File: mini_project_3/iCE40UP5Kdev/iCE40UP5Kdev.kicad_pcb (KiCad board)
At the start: 2 copper layers, 27.2 x 52.8 mm, 51 parts, among them J1 USB4105-GF-A, J2 Left, J3 Right, U1 W25Q32JV, U2 MIC5365-1-2YD5, U3 MIC5318-3-3YD5, U4 ICE40UP5K-SG48ITR, X1 IQXO-791

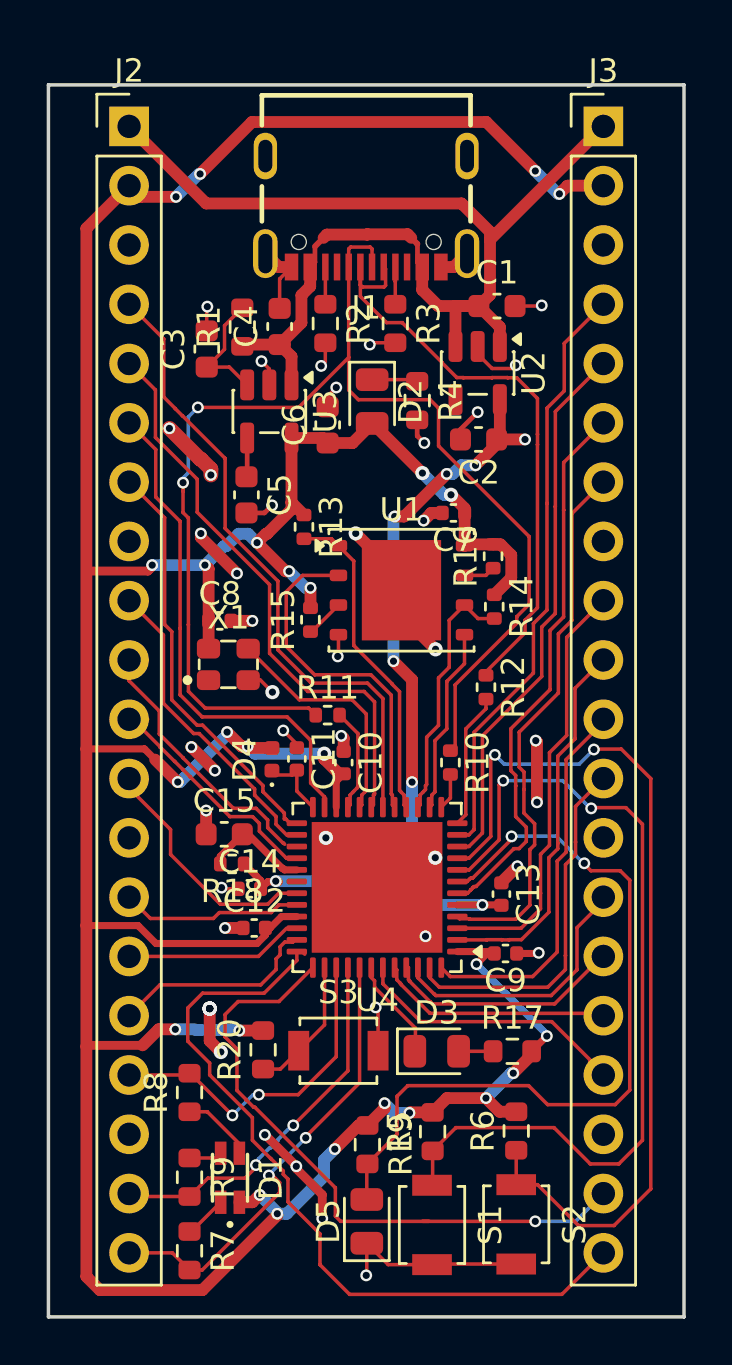
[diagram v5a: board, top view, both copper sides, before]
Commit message: Add silkscreen to mini project 3
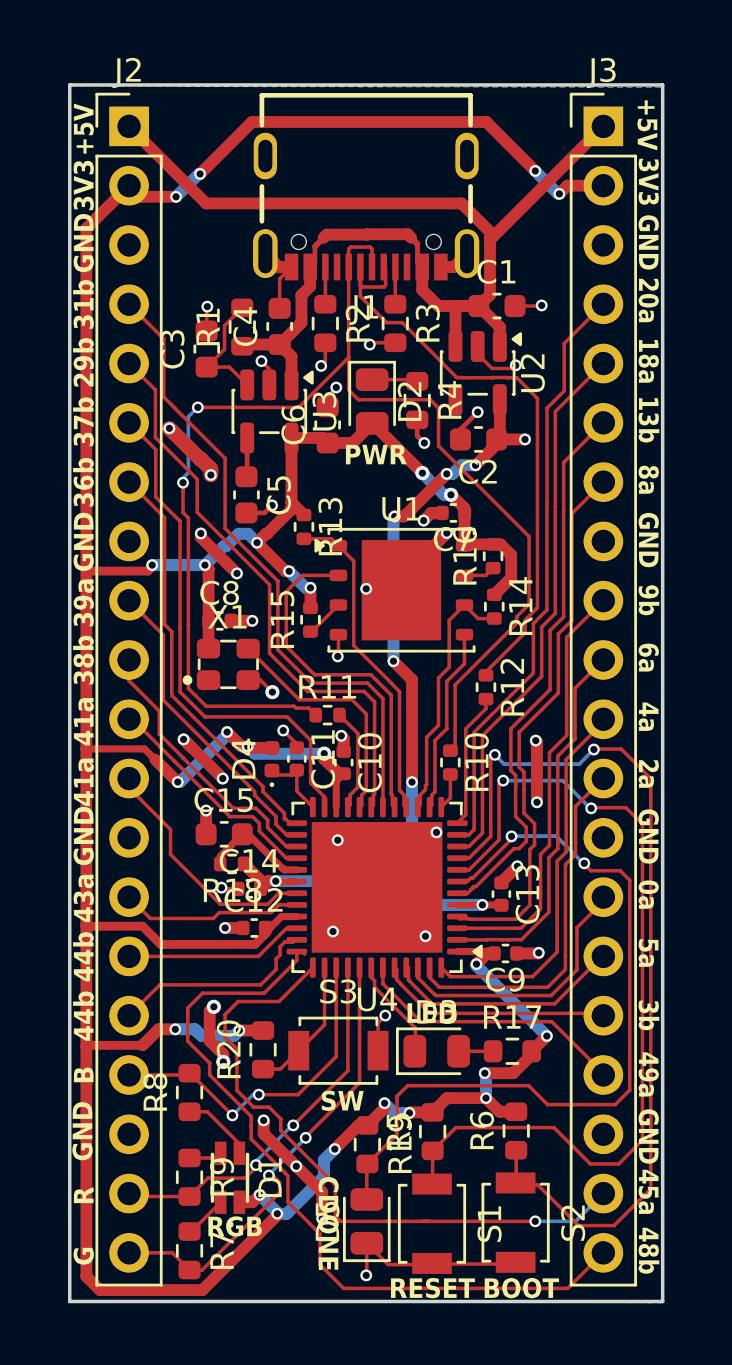
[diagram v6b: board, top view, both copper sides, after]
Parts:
- moved S2 0.08 mm to (156.3, 130.8)
- moved S1 0.05 mm to (152.7, 130.8)
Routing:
- net GND: track 70.3 -> 74.9 mm, vias 44 -> 42
- net +3V3: track 178.3 -> 179.2 mm
- net +1V2: track 39.3 -> 40.0 mm
- net /IOT_38b: track 11.8 -> 12.4 mm
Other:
- board size 27.2 x 52.8 mm -> 25.4 x 52.1 mm
- board text added: "+5V"
- board text added: "0a"
- board text added: "13b"
- board text added: "18a"
- board text added: "20a"
- board text added: "29b"
- board text added: "2a"
- board text added: "31b"
- board text added: "36b"
- board text added: "37b"
- board text added: "38b"
- board text added: "39a"
- board text added: "3V3"
- board text added: "3b"
- board text added: "41a"
- board text added: "43a"
- board text added: "44b"
- board text added: "45a"
- board text added: "48b"
- board text added: "49a"
- board text added: "4a"
- board text added: "5a"
- board text added: "6a"
- board text added: "8a"
- board text added: "9b"
- board text added: "B"
- board text added: "BOOT"
- board text added: "CDONE"
- board text added: "G"
- board text added: "GND"
- board text added: "LED"
- board text added: "PWR"
- board text added: "R"
- board text added: "RESET"
- board text added: "RGB"
- board text added: "SW"

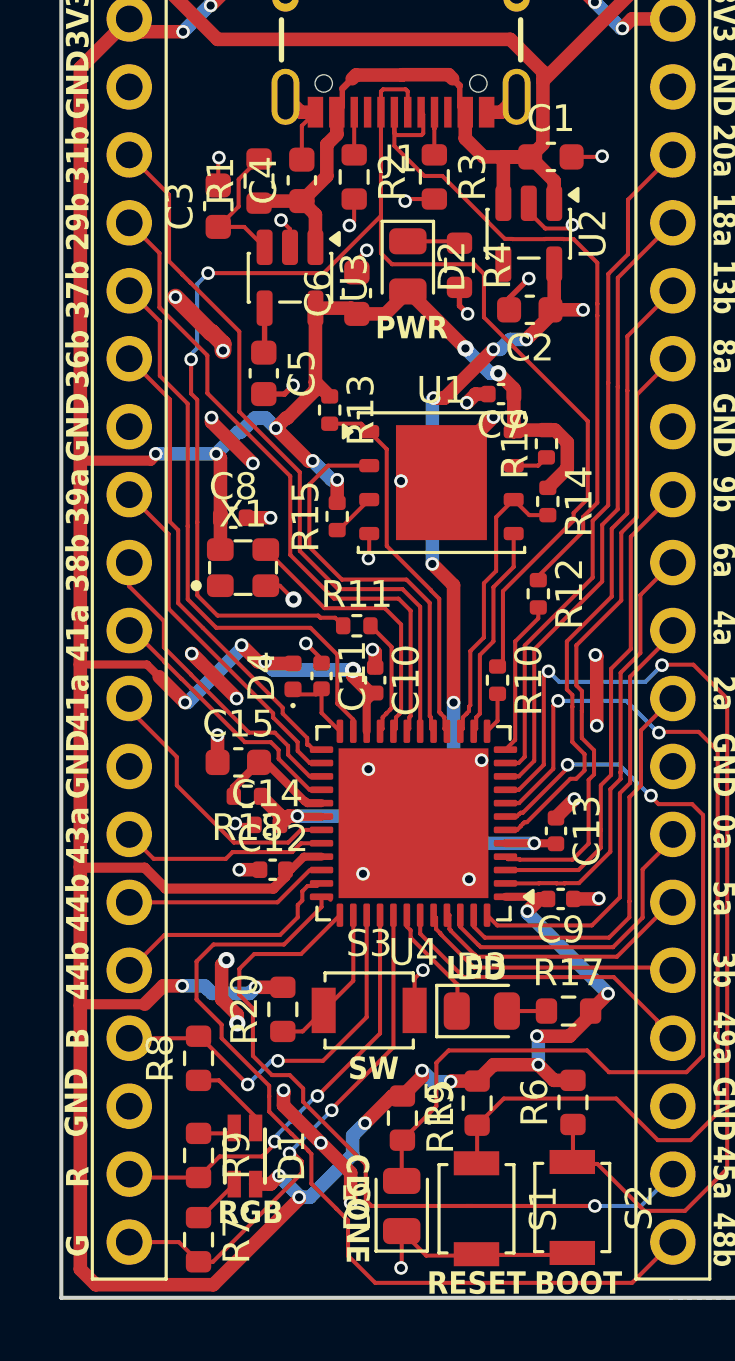
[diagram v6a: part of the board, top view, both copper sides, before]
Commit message: Add more silkscreen for MP3
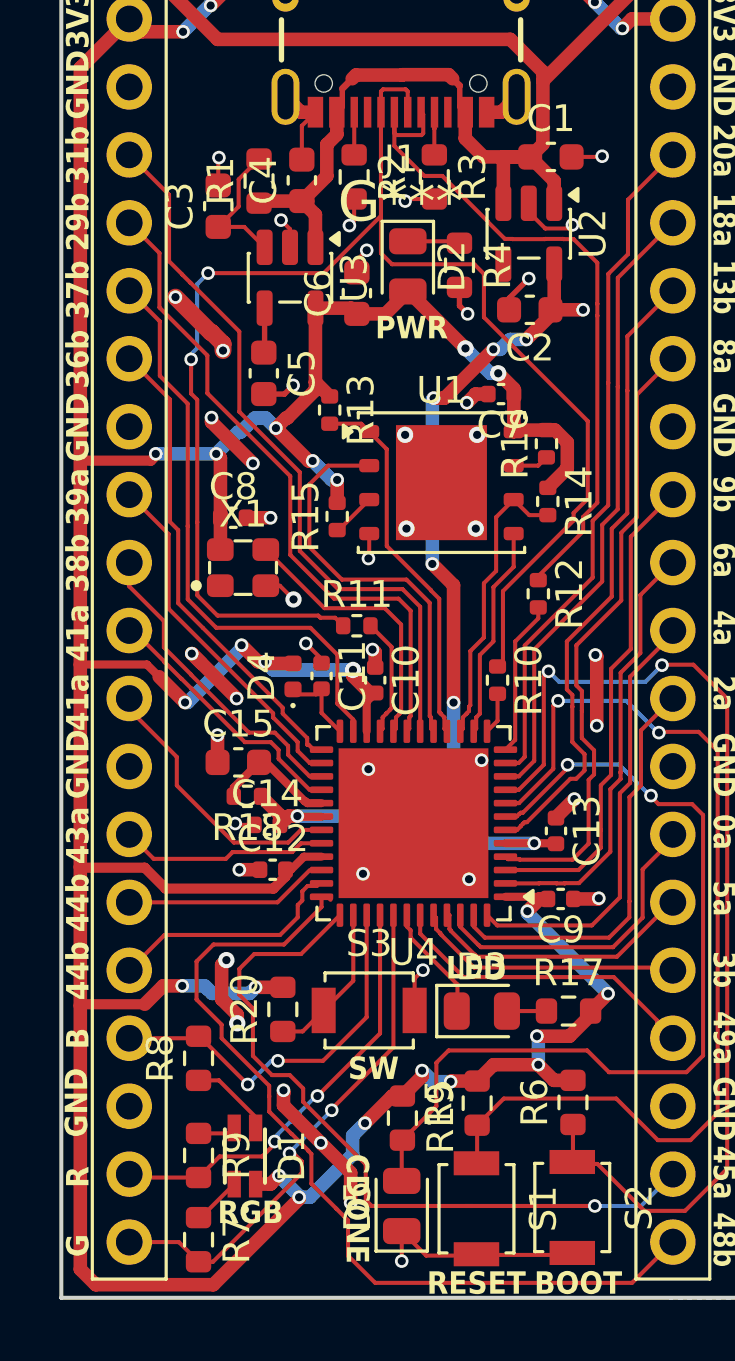
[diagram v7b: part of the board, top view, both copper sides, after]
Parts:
- added G***: LOGO, LOGO, B.Cu at (149.8, 93.2)
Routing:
- net GND: track 74.9 -> 79.0 mm, vias 42 -> 44
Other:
- board text added: "Mark Belanger ice40UP5K Dev Board Eclectronics SP26 Mini Project 3"

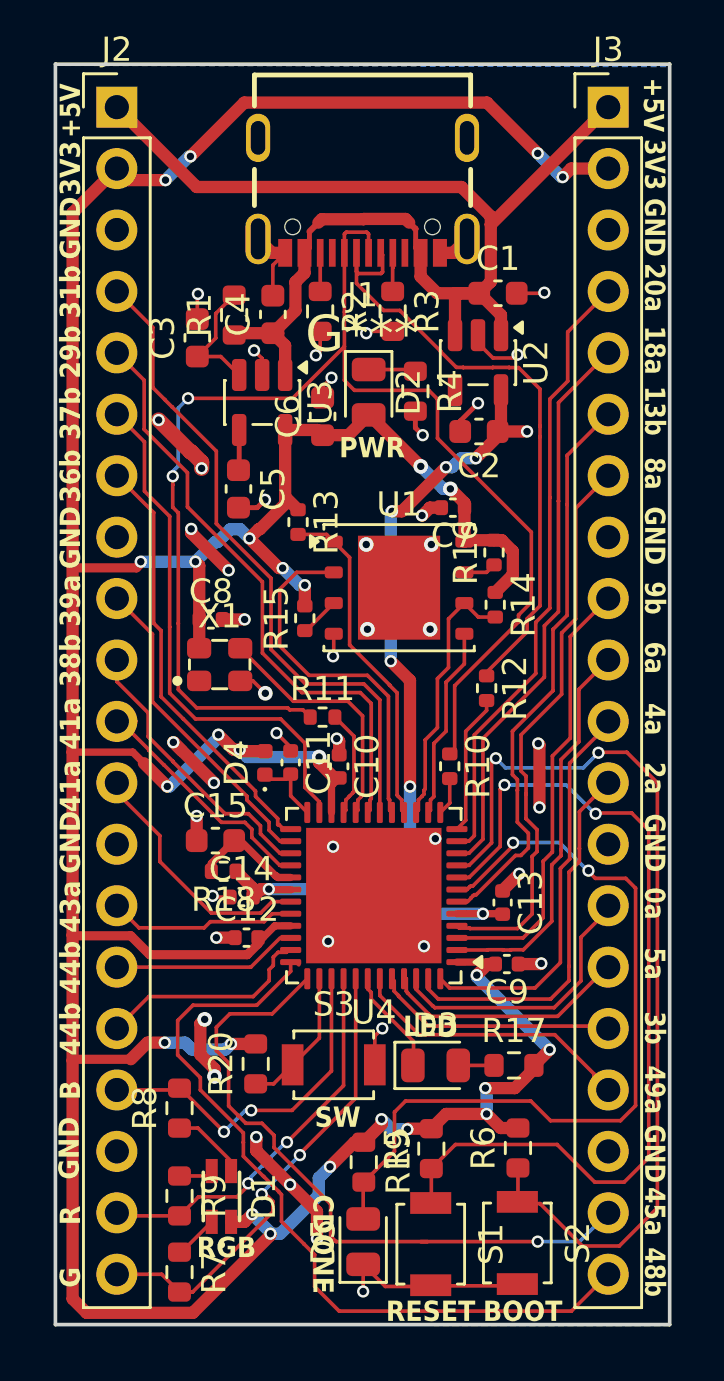
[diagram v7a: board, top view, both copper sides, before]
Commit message: Fix via size, silkscreen, and add README
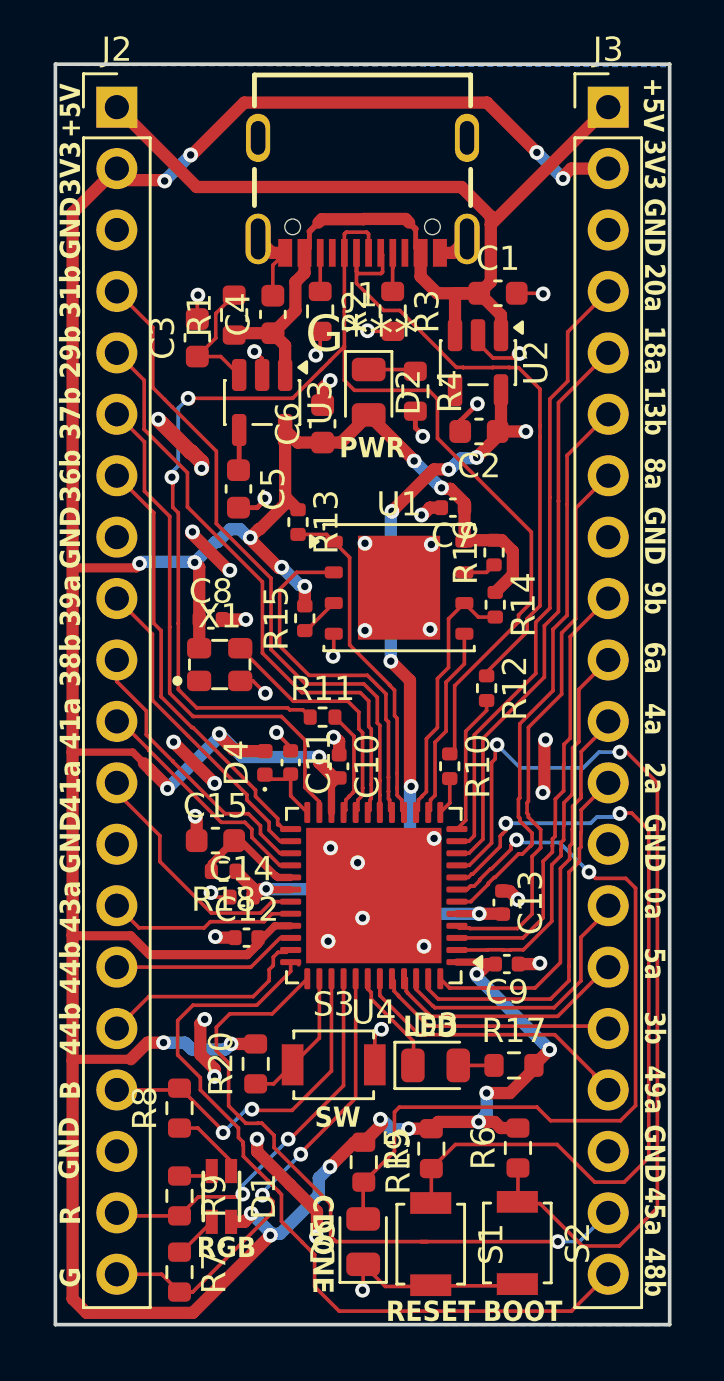
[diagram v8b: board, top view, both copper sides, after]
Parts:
- moved C6 0.30 mm to (148.2, 96.9)
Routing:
- net GND: track 79.0 -> 89.5 mm, vias 44 -> 45
- net +3V3: track 179.2 -> 181.3 mm, vias 26 -> 25
- net Net-(U4-~{CRESET}): track 37.3 -> 35.4 mm
- net /RGB1: track 16.2 -> 17.1 mm
- net /IOT_41a: track 10.7 -> 9.86 mm
- net Net-(U4-IOB_16a): track 39.2 -> 40.0 mm
- net +1V2: track 40.0 -> 40.6 mm
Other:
- board text added: "Mark Belanger iCE40UP5K Dev Board Eclectronics SP26 Mini Project 3 09 March 2026"
- board text removed: "Mark Belanger ice40UP5K Dev Board Eclectronics SP26 Mini Project 3"
